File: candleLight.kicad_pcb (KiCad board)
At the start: 2 copper layers, 37.7 x 20 mm, 44 parts, among them P501 USB_OTG, U201 STM32F072C8Tx, U301 MCP1754ST-3302E/MB, U401 TJA1051/3, X501 CON_SWD, X502 SUB-D9, Y201 8MHz

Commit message: Perform automatic KiCAD rescue operations
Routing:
- net (no net): track 3.10 -> 0.00 mm

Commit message: Add Linux Automation page layout
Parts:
- renumbered TX to W201, RX to W202, SCL to W203, SDA to W204, CS to W205, SCK to W206, MISO to W207, MOSI to W208
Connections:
- FID101 pad ~: (no net) -> Net-(FID101-Pad~)
- FID102 pad ~: (no net) -> Net-(FID102-Pad~)
- FID103 pad ~: (no net) -> Net-(FID103-Pad~)
- P501 pad 4: (no net) -> Net-(P501-Pad4)
- U201 pad 12: (no net) -> Net-(U201-Pad12)
- U201 pad 13: (no net) -> Net-(U201-Pad13)
- U201 pad 14: (no net) -> Net-(U201-Pad14)
- U201 pad 15: (no net) -> Net-(U201-Pad15)
- U201 pad 16: (no net) -> Net-(U201-Pad16)
- U201 pad 17: (no net) -> Net-(U201-Pad17)
- U201 pad 18: (no net) -> Net-(U201-Pad18)
- U201 pad 19: (no net) -> Net-(U201-Pad19)
- U201 pad 20: (no net) -> Net-(U201-Pad20)
- U201 pad 21: (no net) -> Net-(U201-Pad21)
- U201 pad 22: (no net) -> Net-(U201-Pad22)
- U201 pad 29: (no net) -> Net-(U201-Pad29)
- U201 pad 3: (no net) -> Net-(U201-Pad3)
- U201 pad 38: (no net) -> Net-(U201-Pad38)
- U201 pad 39: (no net) -> Net-(U201-Pad39)
- U201 pad 4: (no net) -> Net-(U201-Pad4)
- U201 pad 40: (no net) -> Net-(U201-Pad40)
- U201 pad 41: (no net) -> Net-(U201-Pad41)
- X501 pad 6: (no net) -> Net-(X501-Pad6)

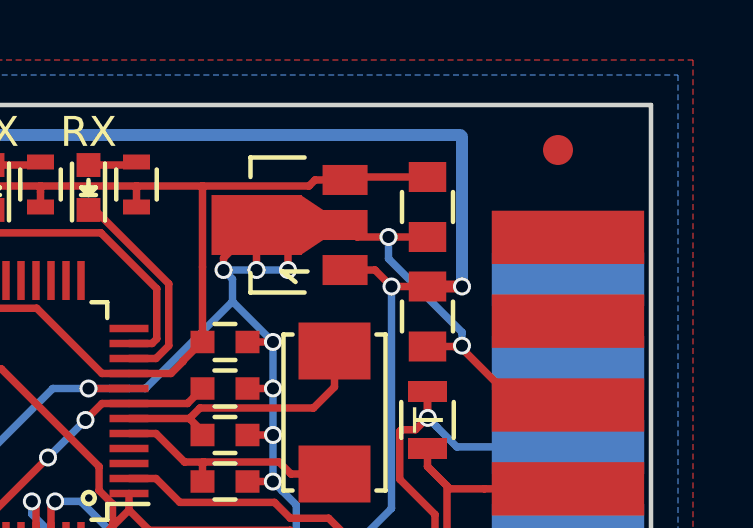
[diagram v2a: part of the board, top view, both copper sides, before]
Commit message: Update Silkscreen and add netnames
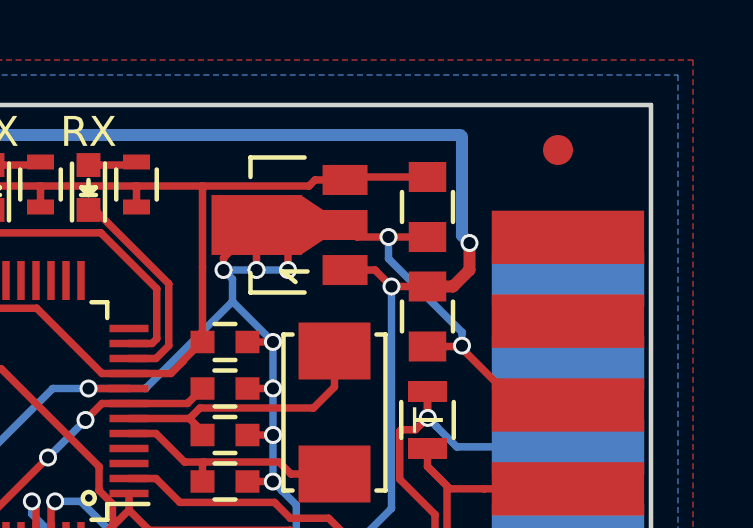
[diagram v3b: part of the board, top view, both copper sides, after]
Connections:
- net Net-(R201-Pad2) renamed /MCU/SCL
- net Net-(R202-Pad1) renamed /MCU/SDA
- net Net-(U201-Pad25) renamed /MCU/CS
- net Net-(U201-Pad26) renamed /MCU/SCK
- net Net-(U201-Pad27) renamed /MCU/MISO
- net Net-(U201-Pad28) renamed /MCU/MOSI
- net Net-(U201-Pad30) renamed /MCU/TX
- net Net-(U201-Pad31) renamed /MCU/RX
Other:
- board text added: "CS"
- board text added: "MISO"
- board text added: "MOSI"
- board text added: "SCK"
- board text added: "SCL"
- board text added: "SDA"
- board text added: "VB+"
- board text added: "candleLight-P01-R01-B01"
- board text added: "https://linux-automation.com"
- board text removed: "candleLight v1.1"
- board text removed: "http://bytewerk.org"

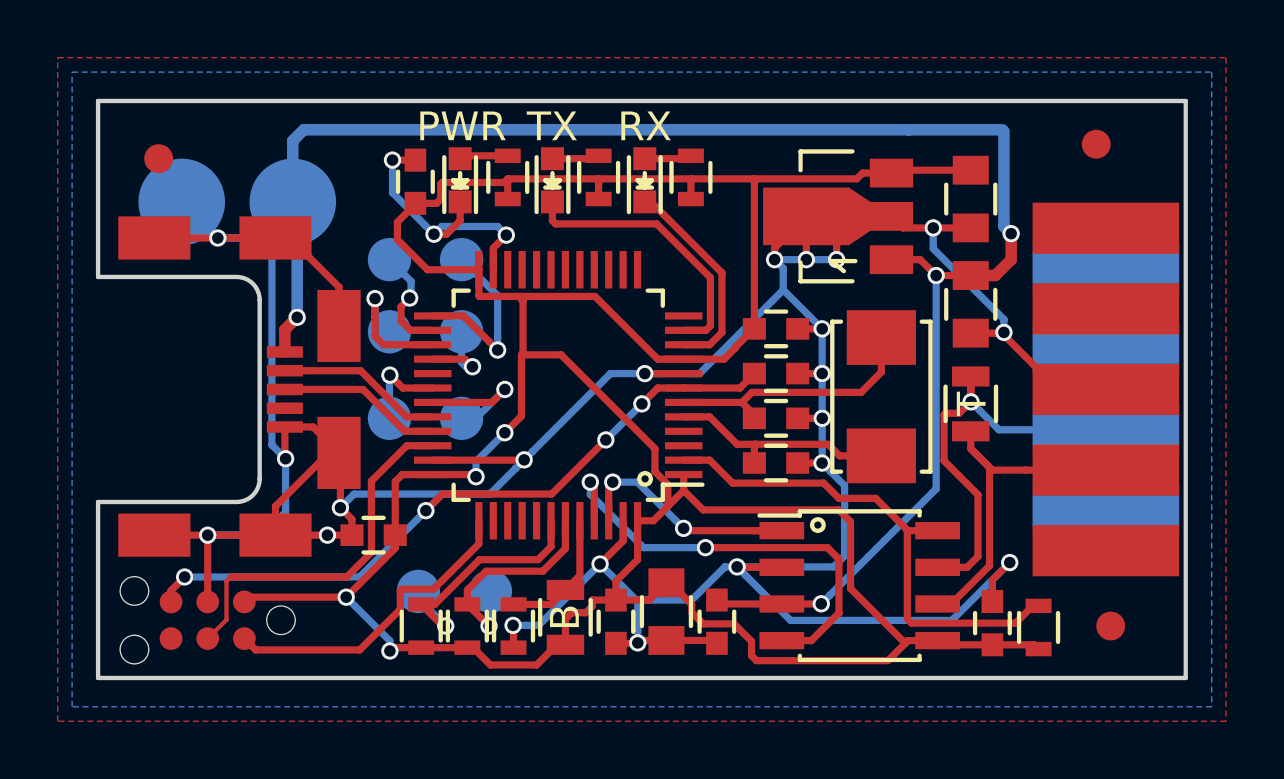
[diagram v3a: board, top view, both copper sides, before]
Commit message: Add Cap voltage rating, Put PCB ref on cupper, add note for variants
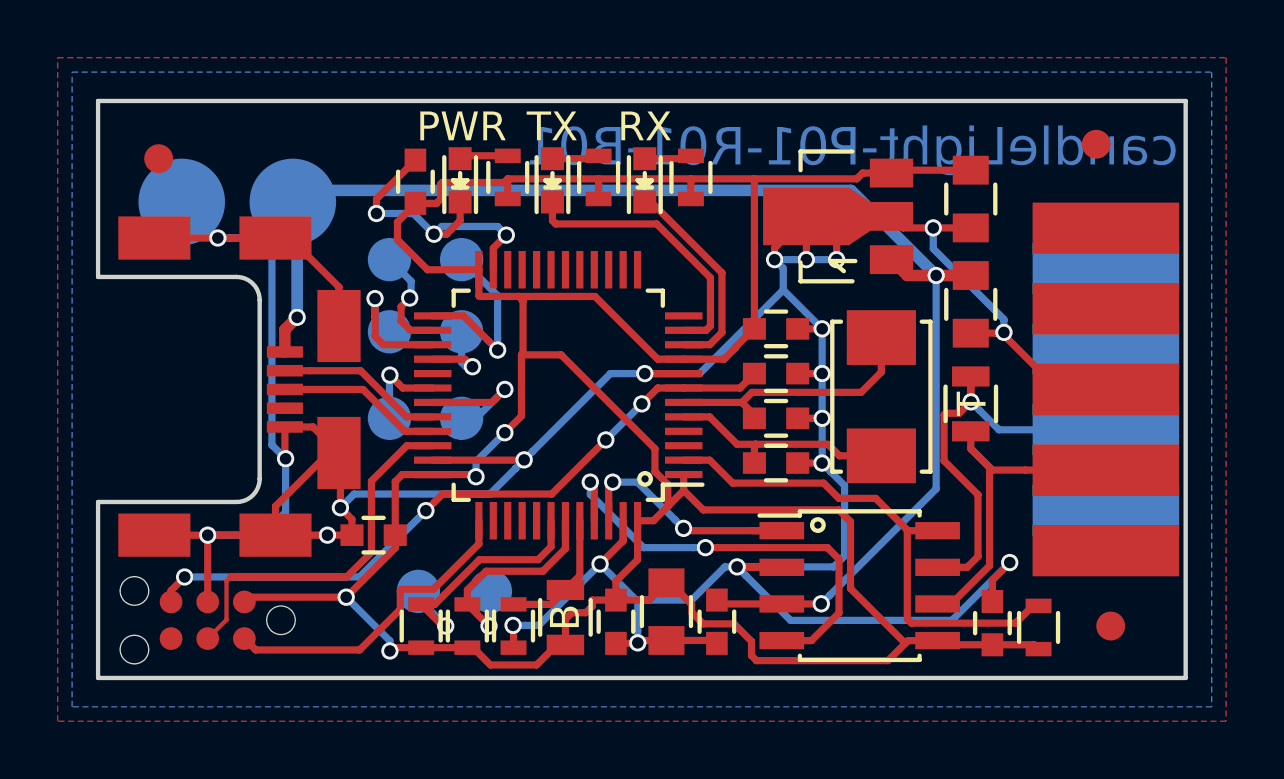
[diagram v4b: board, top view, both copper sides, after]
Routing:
- net +5V: track 58.5 -> 49.0 mm, vias 4 -> 3
- net GND: track 148.8 -> 149.5 mm
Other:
- board text added: "VB-"

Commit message: Add linux automation logo
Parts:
- added NB101: LAG_logo, logo:lag_rocket_10mmx10.4mm, B.Cu at (63.3, 86.1)

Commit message: Create release candlelight-S01-R01
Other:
- rule pad_to_mask_clearance: 0.05 -> 0
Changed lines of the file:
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@@
     (pad_size 1.524 1.524)
     (pad_drill 0.762)
-    (pad_to_mask_clearance 0.05)
+    (pad_to_mask_clearance 0)
     (aux_axis_origin 41.4 95)
     (grid_origin 43.5 75.5)
     (visible_elements FFFFFFFF)
     (pcbplotparams
-      (layerselection 0x010c0_80000001)
+      (layerselection 0x011fc_ffffffff)
       (usegerberextensions true)
       (usegerberattributes true)
       (usegerberadvancedattributes true)
       (creategerberjobfile true)
-      (excludeedgelayer true)
+      (excludeedgelayer false)
       (linewidth 0.100000)
-      (plotframeref false)
+      (plotframeref true)
       (viasonmask false)
       (mode 1)
@@
       (drillshape 0)
       (scaleselection 1)
-      (outputdirectory "gerber/"))
+      (outputdirectory "releases/candlelight-S01-R01/candlelight-P01-R01/gerber/"))
   )
   (net 0 "")
